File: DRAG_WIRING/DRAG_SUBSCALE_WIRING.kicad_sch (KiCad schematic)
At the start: 11 parts, among them J1 Conn_01x02, J3 Conn_01x02, U1 Teensy4.1

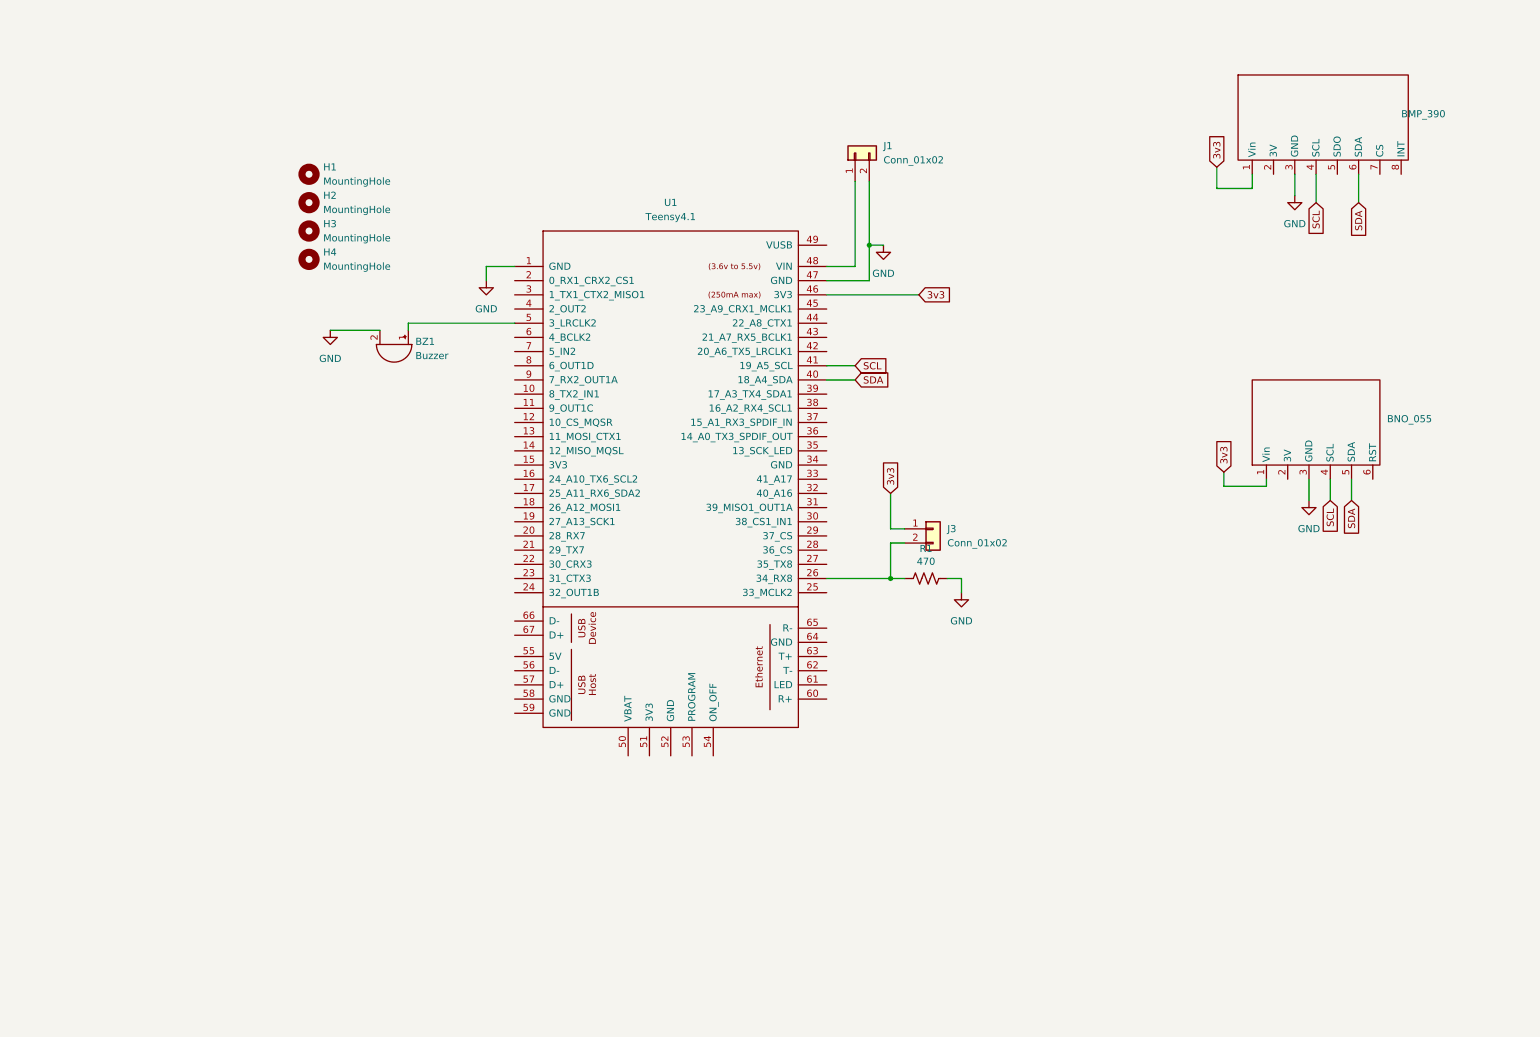
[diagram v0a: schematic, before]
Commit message: updating to fullscale
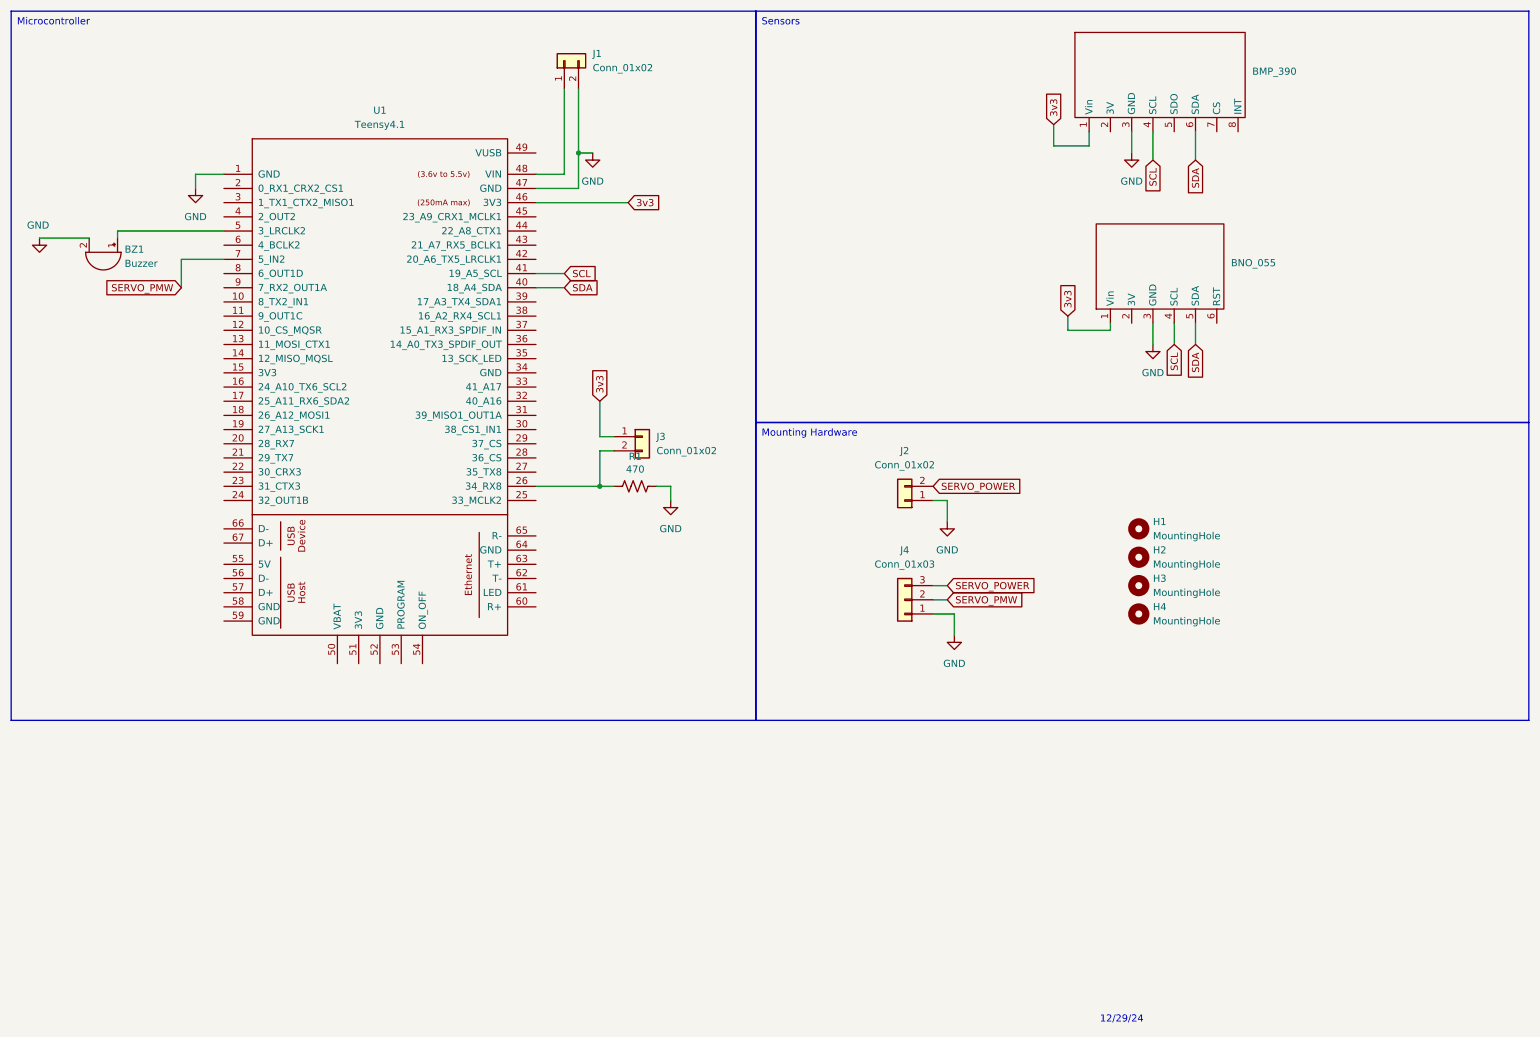
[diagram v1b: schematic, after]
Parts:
- added J2: Conn_01x02, Connector_JST:JST_XA_B02B-XASK-1_1x02_P2.50mm_Vertical, symbol Connector_Generic:Conn_01x02
- added J4: Conn_01x03, Connector_JST:JST_EH_B3B-EH-A_1x03_P2.50mm_Vertical, symbol Connector_Generic:Conn_01x03
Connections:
- net GND: now also J2.1 (Pin_1), J4.1 (Pin_1)
- net SERVO_PMW: now reaches U1.7 (5_IN2)
- net SERVO_PMW: now also J4.2 (Pin_2)
- new net SERVO_POWER: J2.2 (Pin_2), J4.3 (Pin_3)
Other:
- note added: "12/29/24"
- moved on the sheet: BMP_390, BNO_055, BZ1, H1, H2, H3, H4, J1, J3, R1, U1

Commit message: Updating wiring and pcb for servo
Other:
- note added: "Battery Input"
- note added: "Keyswitch pulldown input"
- note added: "Servo Connections"
- note removed: "12/29/24"
- title: (none) -> Drag Wiring
- moved on the sheet: J3
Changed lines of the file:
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@@
 	(generator_version "8.0")
 	(paper "A4")
+	(title_block
+		(title "Drag Wiring")
+		(date "2024-12-29")
+	)
 	(junction
 		(at 114.3 38.1)
@@
 	(wire
 		(pts
+			(xy 118.11 86.36) (xy 120.65 86.36)
+		)
+		(stroke
+			(width 0)
+			(type default)
+		)
+	)
+	(wire
+		(pts
+			(xy 205.74 36.83) (xy 205.74 34.29)
+		)
+		(stroke
+			(width 0)
+			(type default)
+		)
+	)
+	(wire
+		(pts
+			(xy 45.72 44.45) (xy 45.72 41.91)
+		)
+		(stroke
+			(width 0)
+			(type default)
+		)
+	)
+	(wire
+		(pts
 			(xy 118.11 88.9) (xy 120.65 88.9)
 		)
@@
 	(wire
 		(pts
-			(xy 205.74 36.83) (xy 205.74 34.29)
-		)
-		(stroke
-			(width 0)
-			(type default)
-		)
-	)
-	(wire
-		(pts
-			(xy 45.72 44.45) (xy 45.72 41.91)
-		)
-		(stroke
-			(width 0)
-			(type default)
-		)
-	)
-	(wire
-		(pts
-			(xy 118.11 91.44) (xy 120.65 91.44)
-		)
-		(stroke
-			(width 0)
-			(type default)
-		)
-	)
-	(wire
-		(pts
 			(xy 50.8 57.15) (xy 43.18 57.15)
 		)
@@
 	(wire
 		(pts
-			(xy 118.11 91.44) (xy 118.11 97.79)
-		)
-		(stroke
-			(width 0)
-			(type default)
-		)
-	)
-	(wire
-		(pts
-			(xy 118.11 82.55) (xy 118.11 88.9)
+			(xy 118.11 88.9) (xy 118.11 97.79)
+		)
+		(stroke
+			(width 0)
+			(type default)
+		)
+	)
+	(wire
+		(pts
+			(xy 118.11 80.01) (xy 118.11 86.36)
 		)
 		(stroke
@@
 		)
 	)
-	(text_box "Mounting Hardware\n"
+	(text_box "External Hardware\n"
 		(exclude_from_sim no)
 		(at 146.05 86.36 0)
@@
 		)
 	)
-	(text "12/29/24"
+	(text "Servo Connections"
 		(exclude_from_sim no)
-		(at 211.582 193.294 0)
+		(at 157.226 106.934 0)
+		(effects
+			(font
+				(size 1.27 1.27)
+			)
+		)
+	)
+	(text "Keyswitch pulldown input"
+		(exclude_from_sim no)
+		(at 132.334 80.518 0)
+		(effects
+			(font
+				(size 1.27 1.27)
+			)
+		)
+	)
+	(text "Battery Input\n"
+		(exclude_from_sim no)
+		(at 113.03 18.034 0)
 		(effects
 			(font
@@
 	(global_label "3v3"
 		(shape input)
-		(at 118.11 82.55 90)
+		(at 118.11 80.01 90)
 		(fields_autoplaced yes)
 		(effects
@@
 		)
 		(property "Intersheetrefs" "${INTERSHEET_REFS}"
-			(at 118.11 76.1782 90)
+			(at 118.11 73.6382 90)
 			(effects
 				(font
@@
 	(symbol
 		(lib_id "Connector_Generic:Conn_01x02")
-		(at 125.73 88.9 0)
+		(at 125.73 86.36 0)
 		(unit 1)
 		(exclude_from_sim no)
@@
 		(fields_autoplaced yes)
 		(property "Reference" "J3"
+			(at 128.27 86.3599 0)
+			(effects
+				(font
+					(size 1.27 1.27)
+				)
+				(justify left)
+			)
+		)
+		(property "Value" "Conn_01x02"
 			(at 128.27 88.8999 0)
 			(effects
@@
 			)
 		)
-		(property "Value" "Conn_01x02"
-			(at 128.27 91.4399 0)
-			(effects
-				(font
-					(size 1.27 1.27)
-				)
-				(justify left)
-			)
-		)
 		(property "Footprint" "Connector_JST:JST_XA_B02B-XASK-1_1x02_P2.50mm_Vertical"
-			(at 125.73 88.9 0)
+			(at 125.73 86.36 0)
 			(effects
 				(font
@@
 		)
 		(property "Datasheet" "~"
-			(at 125.73 88.9 0)
+			(at 125.73 86.36 0)
 			(effects
 				(font
@@
 		)
 		(property "Description" "Generic connector, single row, 01x02, script generated (kicad-library-utils/schlib/autogen/connector/)"
-			(at 125.73 88.9 0)
-			(effects
-				(font
+			(at 125.73 86.36 0)
+			(effects
+				(font
